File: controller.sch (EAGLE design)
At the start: 26 parts, among them SW1 EC12E_SW, U1 LCD-16X2NOHOLES

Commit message: Simplified controller design, internal arduino pullup resistors can be used.
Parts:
- removed R2: 47k, rcl:R-EU_M0805
- removed R4, R5: 100R, rcl:R-EU_M0805
- removed RN1: 10k, resistor-dil:4R-N0603-ARC
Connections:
- removed net N$13: IO2.2, R5.2
- removed net SENSOR1: IO1.2, R4.2
- new net V+: POWER.2, R1.CCW, U1.VDD
- net +5V: no longer PHOTOCELL.P$2, POWER.2, R1.CCW, RN1A.2, RN1B.2, RN1C.2, RN1D.2, U1.VDD
- net EXTRA_IO1: now also IO1.2; no longer R4.1
- net EXTRA_IO2: now also IO2.2; no longer R5.1
- net GND: now also PHOTOCELL.P$1; no longer R2.1
- net LIGHTLEVEL: now also PHOTOCELL.P$2; no longer PHOTOCELL.P$1, R2.2
- net ROTARY_A: no longer RN1C.1
- net ROTARY_B: no longer RN1D.1
- net ROTARY_PUSH: no longer RN1B.1
- net SHAKE_SENSOR: no longer RN1A.1
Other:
- note added: "Battery Connector 4.8 - 6V"
- note added: "Turn Wheel"
- note added: "Vibration sensor"
- note removed: "Power Connector 3.6 - 6 V"
- moved on the sheet: C15, IO1, IO2, PHOTOCELL, S1, SW1

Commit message: Working on controller board. Simplified scamea a bit.
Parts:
- removed C11: 100 uF, rcl:CPOL-EUE2.5-6
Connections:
- net +3V3: no longer C11.+
- net GND: no longer C11.-
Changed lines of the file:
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@@
 <part name="C10" library="rcl" deviceset="C-EU" device="C0805" value="100 nF"/>
 <part name="+3V1" library="supply1" deviceset="+3V3" device=""/>
-<part name="C11" library="rcl" deviceset="CPOL-EU" device="E2.5-6" value="100 uF"/>
 <part name="SUPPLY42" library="supply2" deviceset="GND" device=""/>
 <part name="+3V2" library="supply1" deviceset="+3V3" device=""/>
@@
 <instance part="C10" gate="G$1" x="17.78" y="-86.36"/>
 <instance part="+3V1" gate="G$1" x="17.78" y="-76.2"/>
-<instance part="C11" gate="G$1" x="30.48" y="-86.36"/>
 <instance part="SUPPLY42" gate="GND" x="35.56" y="53.34"/>
 <instance part="+3V2" gate="G$1" x="-38.1" y="58.42"/>
@@
 <pinref part="SUPPLY40" gate="GND" pin="GND"/>
 <pinref part="C10" gate="G$1" pin="2"/>
-<pinref part="C11" gate="G$1" pin="-"/>
-<wire x1="30.48" y1="-91.44" x2="17.78" y2="-91.44" width="0.1524" layer="91"/>
-<junction x="17.78" y="-91.44"/>
 </segment>
 <segment>
@@
 <pinref part="+3V1" gate="G$1" pin="+3V3"/>
 <wire x1="17.78" y1="-78.74" x2="17.78" y2="-83.82" width="0.1524" layer="91"/>
-<junction x="17.78" y="-83.82"/>
-<pinref part="C11" gate="G$1" pin="+"/>
-<wire x1="30.48" y1="-83.82" x2="17.78" y2="-83.82" width="0.1524" layer="91"/>
-<junction x="17.78" y="-83.82"/>
-</segment>
-<segment>
+</segment>
+<segment>

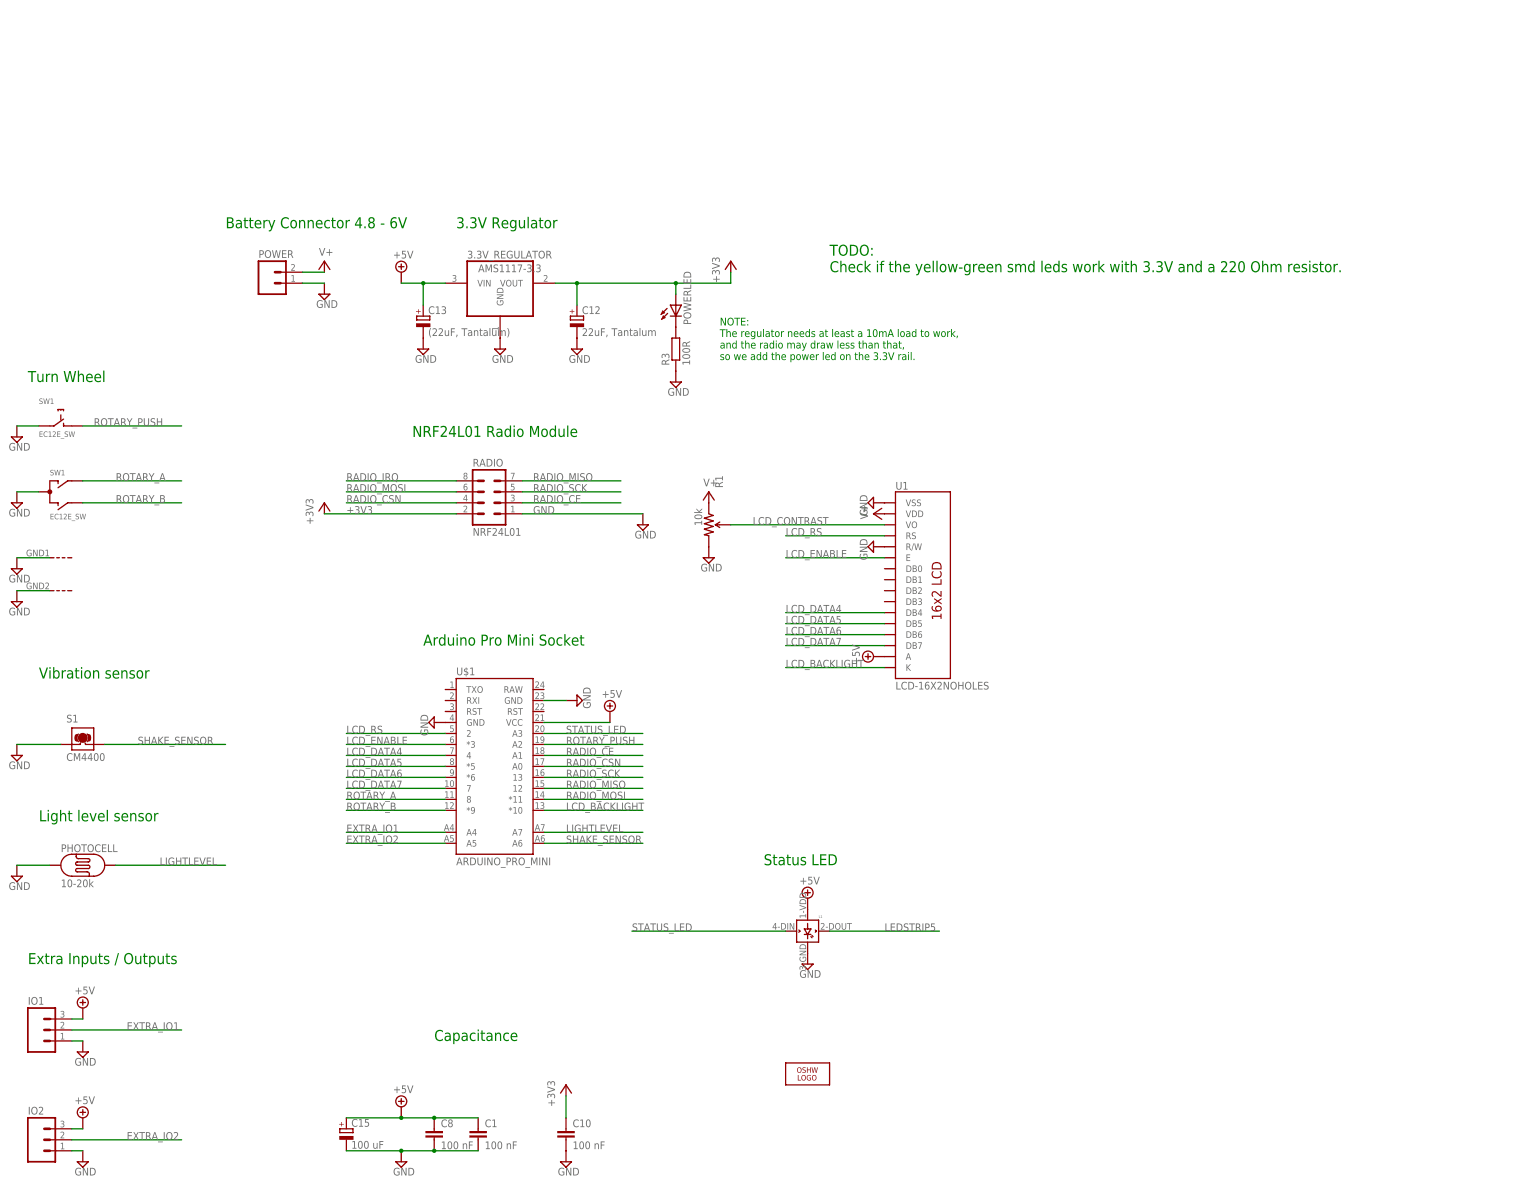
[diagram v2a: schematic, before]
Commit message: Started working on smaller ledboard. Some updates to controll board.
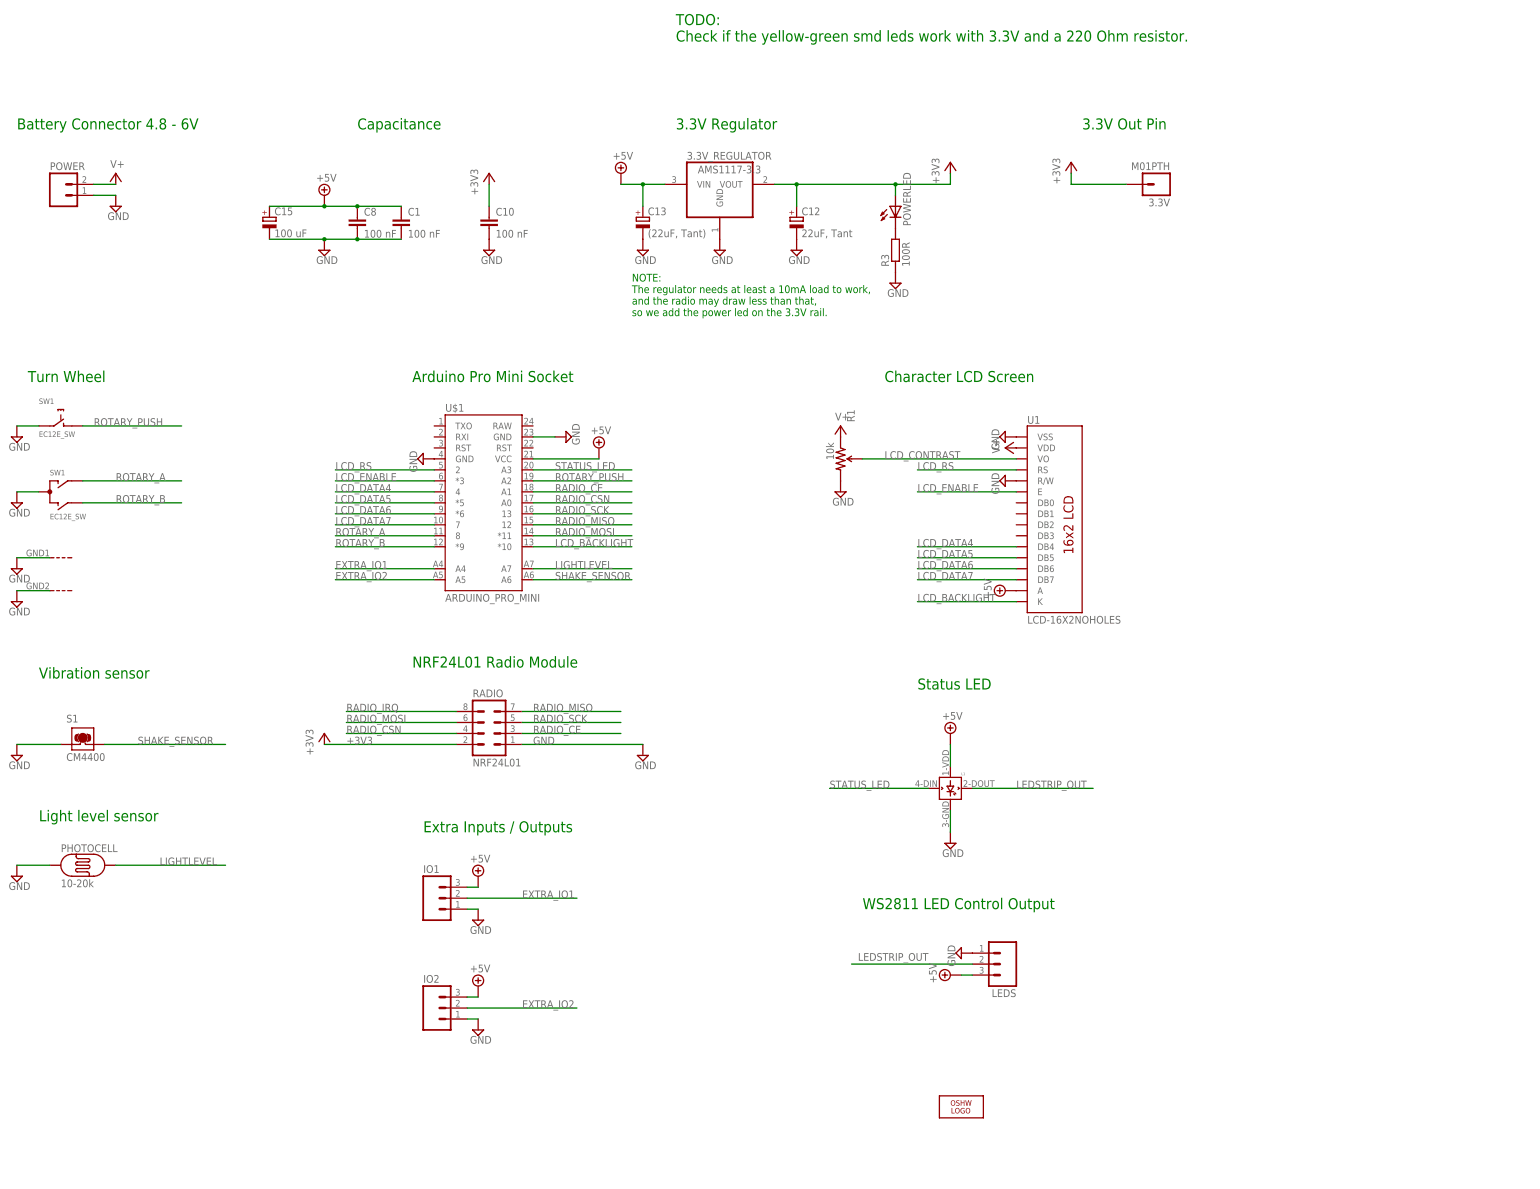
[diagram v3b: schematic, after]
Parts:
- added 3.3V: M01PTH, SparkFun-Connectors:M01PTH
- added LEDS: (no value), SparkFun-Connectors:M03PTH
- C12: value 22uF, Tantalum -> 22uF, Tant
- C13: value (22uF, Tantalum) -> (22uF, Tant)
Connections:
- removed net LEDSTRIP5: L1.DOUT
- new net LEDSTRIP_OUT: L1.DOUT, LEDS.2
- net +3V3: now also 3.3V.1
- net +5V: now also LEDS.3
- net GND: now also LEDS.1
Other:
- note added: "3.3V Out Pin"
- note added: "Character LCD Screen"
- note added: "WS2811 LED Control Output"
- moved on the sheet: 3.3V_REGULATOR, C1, C10, C12, C13, C15, C8, IO1, IO2, L1, POWER, POWERLED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
